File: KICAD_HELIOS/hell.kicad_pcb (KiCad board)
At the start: 4 copper layers, 109 x 86 mm, 171 parts, among them J101 NC3FAAH, J102 NC3MAAH, J103 ecran, J104 Conn_ST_STDC14, J105 Conn_01x02, SW101 SW_Push, SW102 SW_Push, SW103 SW_Push, U101 R-78B5.0-2.0, U102 AMS1117-3.3, U103 MAX485E, U104 STM32F103C6Tx, U1101 LM3404MA, U1102 LM3404MA, U1103 LM3404MA, U201 LM3404MA, U202 LM3404MA, U203 LM3404MA

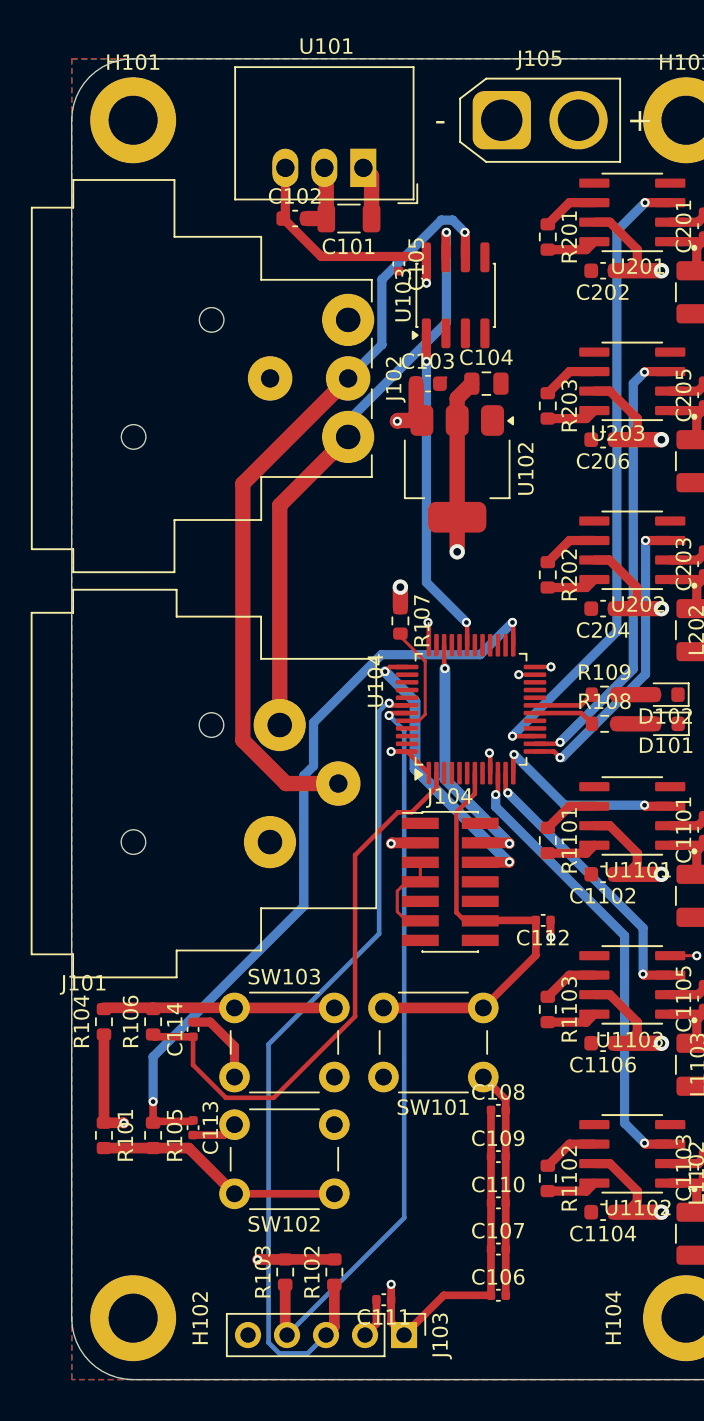
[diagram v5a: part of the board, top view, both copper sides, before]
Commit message: Routage PCB en prenant en compte la place mécanique des composants
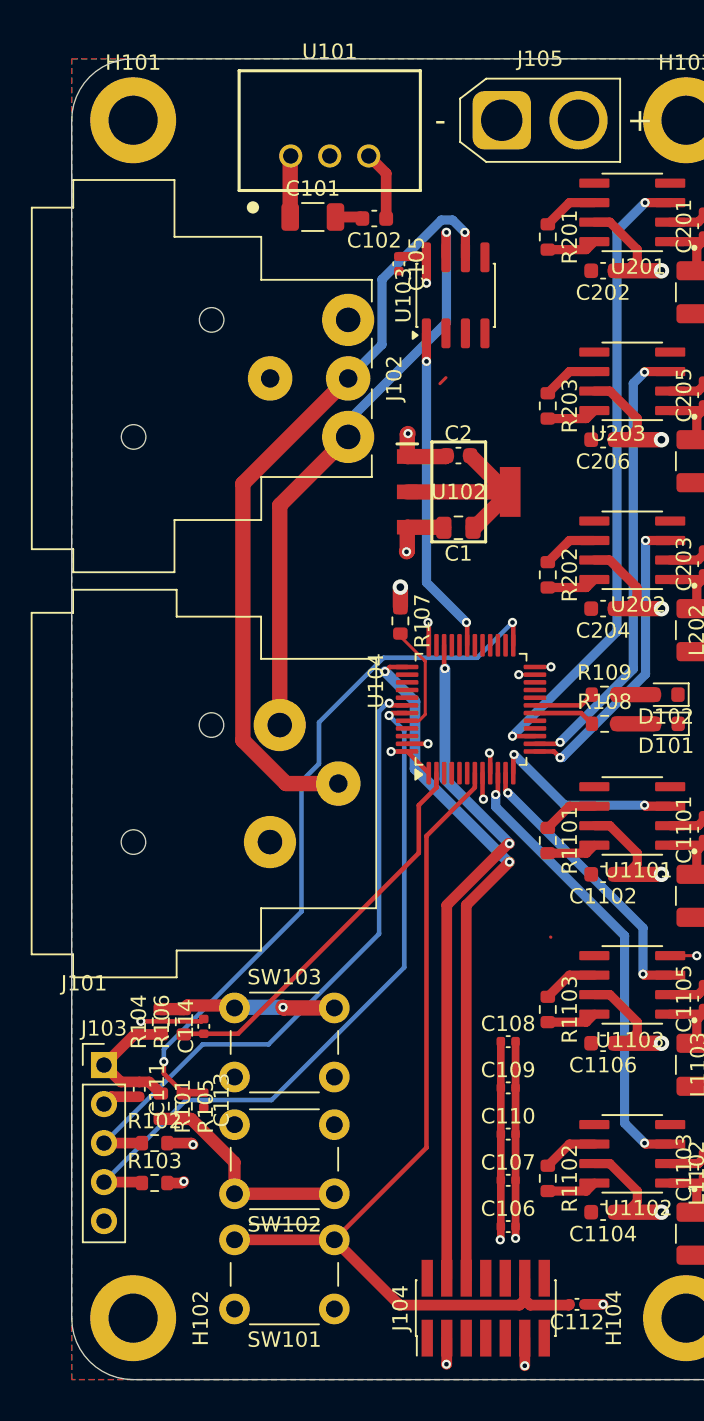
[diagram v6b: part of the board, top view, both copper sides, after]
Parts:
- removed C103: 10u, Capacitor_SMD:C_0603_1608Metric
- removed C104: 22u, Capacitor_SMD:C_0805_2012Metric
- added C1: 22u, Capacitor_SMD:C_0805_2012Metric, F.Cu at (111.2, 66.5)
- added C2: 10u, Capacitor_SMD:C_0603_1608Metric, F.Cu at (111.2, 61.8)
- U101: footprint Converter_DCDC:Converter_DCDC_RECOM_R-78B-2.0_THT -> WPME-FDSM_SIP-3:WPME-FDSM_173950536
- U102: value AMS1117-3.3 -> AZ1117CH2-3.3TRG1; footprint Package_TO_SOT_SMD:SOT-223-3_TabPin2 -> AZ1117CH2-3.3TRG1:SOT230P700X180-4N
- moved J104 27.9 mm to (113.0, 117.3), turned to 90 degrees
- moved J103 26.3 mm to (88.1, 101.5), turned to 0 degrees
- moved C112 25.1 mm to (118.9, 117.1)
- moved C111 21.0 mm to (90.4, 103.1), turned to -90 degrees
- moved SW101 17.9 mm to (103.1, 117.4)
- moved R102 14.4 mm to (91.4, 106.6), turned to 0 degrees
- moved R103 10.3 mm to (91.4, 109.2), turned to 0 degrees
- moved C102 5.15 mm to (105.7, 46.4), turned to 180 degrees
- moved C106 4.52 mm to (114.4, 112.0)
- moved C109 4.52 mm to (114.4, 103.0)
- moved C107 4.52 mm to (114.4, 109.0)
- moved C108 4.52 mm to (114.4, 100.0)
- moved C110 4.52 mm to (114.4, 106.0)
- moved R101 4.16 mm to (91.8, 104.2)
- moved R104 3.70 mm to (91.8, 98.7)
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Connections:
- U102 pad 1: GND -> +5V
- U102 pad 2: +3.3V -> GND
- U102 pad 3: +5V -> +3.3V
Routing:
- net NRST: track 28.6 -> 59.5 mm
- net SWDIO: track 16.6 -> 44.7 mm
- net SWCLK: track 19.3 -> 45.6 mm
- net +3.3V: track 54.7 -> 37.4 mm
- net +5V: track 19.6 -> 33.6 mm
- net Ecr_SCL: track 54.2 -> 42.6 mm
- net BOUTTON_1: track 36.7 -> 25.9 mm
- net +24V: track 145.9 -> 152.0 mm
- net Net-(R104-Pad2): track 15.0 -> 11.5 mm, vias 0 -> 1
- net GND: track 157.1 -> 160.6 mm, vias 46 -> 51
- net BOUTTON_2: track 50.1 -> 47.0 mm
- net Ecr_SDA: track 48.5 -> 45.9 mm
- net Net-(R101-Pad2): track 16.2 -> 14.5 mm

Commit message: PCB
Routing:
- net GND: track 160.6 -> 160.0 mm, vias 51 -> 57
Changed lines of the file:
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@@
-	)
-	(segment
-		(start 110.365 56.76)
-		(end 109.975 57.15)
-		(width 0.2)
-		(layer "F.Cu")
-		(net 1)
 	)
 	(segment
@@
 	)
 	(via
+		(at 118.8 49.8)
+		(size 0.6)
+		(drill 0.3)
+		(layers "F.Cu" "B.Cu")
+		(free yes)
+		(net 1)
+	)
+	(via
 		(at 187.1 77.5)
 		(size 1)
@@
 	)
 	(via
+		(at 112.9 47.2)
+		(size 0.6)
+		(drill 0.3)
+		(layers "F.Cu" "B.Cu")
+		(free yes)
+		(net 1)
+	)
+	(via
 		(at 187.1 41.5)
 		(size 1)
@@
 	)
 	(via
+		(at 111.6 55.5)
+		(size 0.6)
+		(drill 0.3)
+		(layers "F.Cu" "B.Cu")
+		(free yes)
+		(net 1)
+	)
+	(via
+		(at 110.4 55.5)
+		(size 0.6)
+		(drill 0.3)
+		(layers "F.Cu" "B.Cu")
+		(free yes)
+		(net 1)
+	)
+	(via
 		(at 187.1 86.5)
 		(size 1)
@@
 	)
 	(via
+		(at 126.7 44.1)
+		(size 0.6)
+		(drill 0.3)
+		(layers "F.Cu" "B.Cu")
+		(free yes)
+		(net 1)
+	)
+	(via
 		(at 187.1 98.5)
 		(size 1)
@@
 		(net 1)
 	)
+	(via
+		(at 111.6 55.5)
+		(size 0.6)
+		(drill 0.3)
+		(layers "F.Cu" "B.Cu")
+		(free yes)
+		(net 1)
+	)
